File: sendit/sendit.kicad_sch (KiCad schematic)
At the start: 11 parts

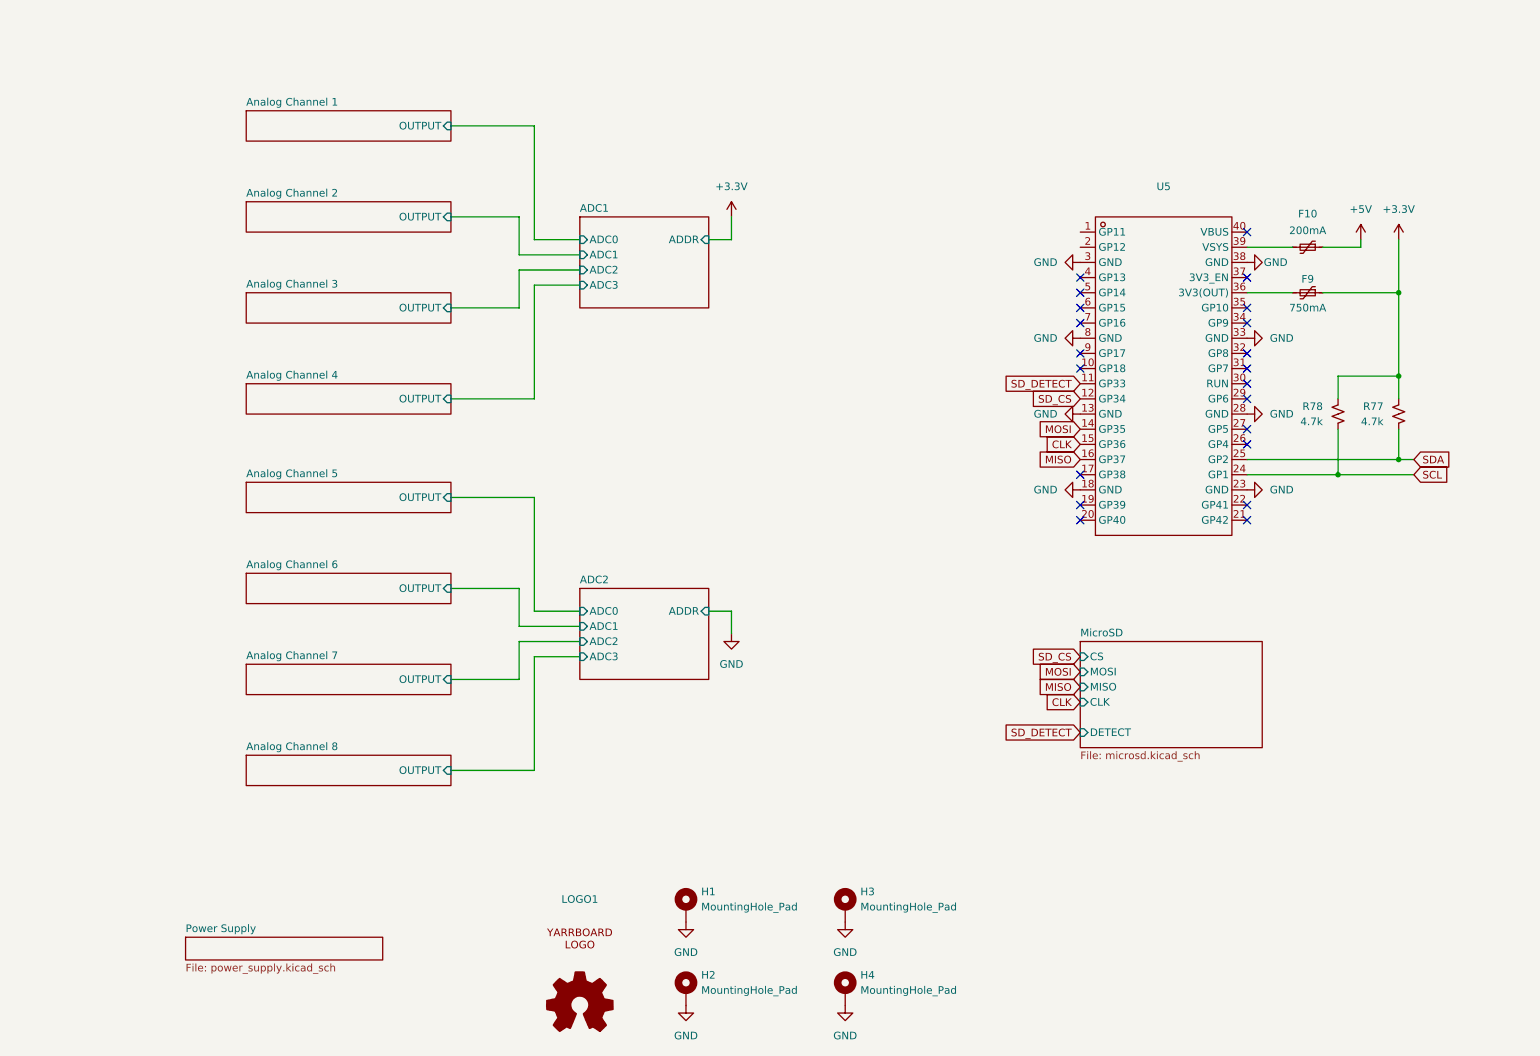
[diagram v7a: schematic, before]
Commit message: test run of jlcpcb upload looks good.
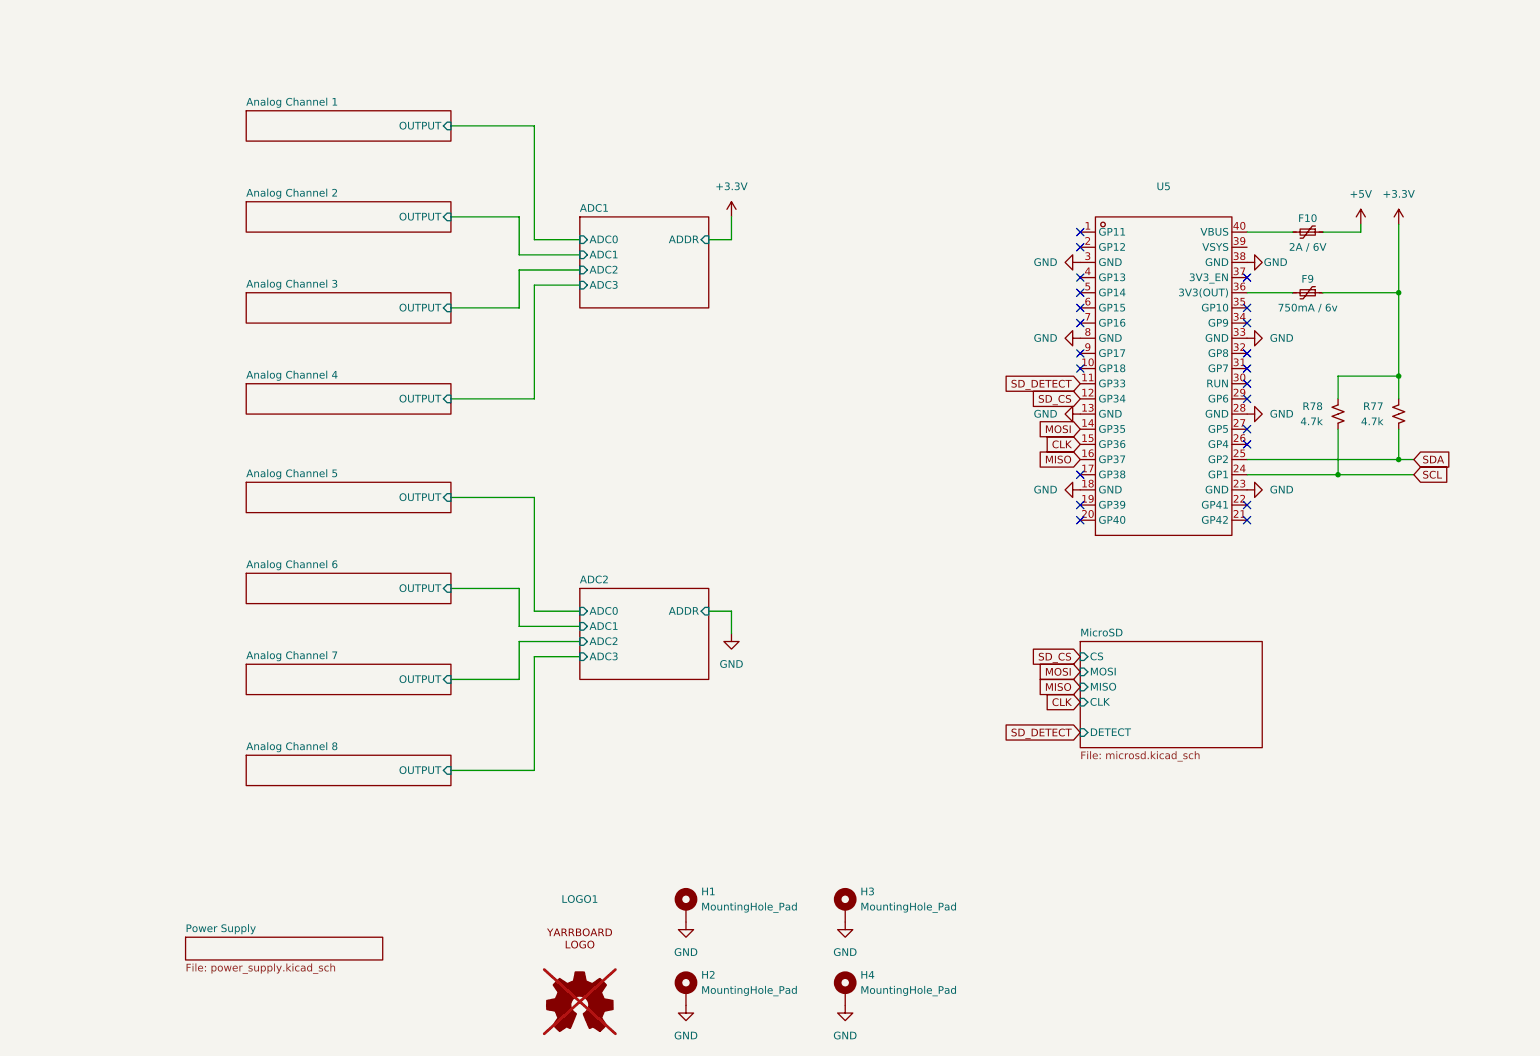
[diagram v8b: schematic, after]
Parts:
- F10: value 200mA -> 2A / 6V; LCSC C126816 -> C914095
- F9: value 750mA -> 750mA / 6v
- LOGO1, LOGO2: now not fitted
- R77, R78: LCSC (none) -> C23162
- U5: LCSC (none) -> C18198404
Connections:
- net at U5.39 (VSYS): no longer F10.2
- net at U5.40 (VBUS): now also F10.2
- no-connect marks 21 -> 22
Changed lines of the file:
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@@
+	)
+	(no_connect
+		(at 191.77 62.23)
 	)
 	(no_connect
@@
 	)
 	(no_connect
-		(at 219.71 59.69)
+		(at 191.77 59.69)
 	)
 	(no_connect
@@
 	(wire
 		(pts
-			(xy 219.71 62.23) (xy 227.33 62.23)
+			(xy 219.71 59.69) (xy 227.33 59.69)
 		)
 		(stroke
@@
 	(wire
 		(pts
-			(xy 238.76 62.23) (xy 238.76 60.96)
-		)
-		(stroke
-			(width 0)
-			(type default)
-		)
-	)
-	(wire
-		(pts
-			(xy 232.41 62.23) (xy 238.76 62.23)
+			(xy 238.76 59.69) (xy 238.76 58.42)
+		)
+		(stroke
+			(width 0)
+			(type default)
+		)
+	)
+	(wire
+		(pts
+			(xy 232.41 59.69) (xy 238.76 59.69)
 		)
 		(stroke
@@
 	(wire
 		(pts
-			(xy 245.11 60.96) (xy 245.11 69.85)
+			(xy 245.11 58.42) (xy 245.11 69.85)
 		)
 		(stroke
@@
 			)
 		)
-		(property "LCSC" ""
+		(property "LCSC" "C23162"
 			(at 234.95 90.17 0)
 			(effects
@@
 			)
 		)
+		(property "LCSC" "C18198404"
+			(at 205.74 83.82 0)
+			(effects
+				(font
+					(size 1.27 1.27)
+				)
+				(hide yes)
+			)
+		)
 		(pin "3"
 		)
@@
 		(in_bom no)
 		(on_board yes)
-		(dnp no)
+		(dnp yes)
 		(fields_autoplaced yes)
 		(property "Reference" "LOGO1"
@@
 	(symbol
 		(lib_id "power:+5V")
-		(at 238.76 60.96 0)
+		(at 238.76 58.42 0)
 		(mirror y)
 		(unit 1)
@@
 		(on_board yes)
 		(dnp no)
-		(fields_autoplaced yes)
 		(property "Reference" "#PWR03"
-			(at 238.76 64.77 0)
+			(at 238.76 62.23 0)
 			(effects
 				(font
@@
 		)
 		(property "Value" "+5V"
-			(at 238.76 55.88 0)
+			(at 238.76 53.34 0)
 			(effects
 				(font
@@
 		)
 		(property "Footprint" ""
-			(at 238.76 60.96 0)
+			(at 238.76 58.42 0)
 			(effects
 				(font
@@
 		)
 		(property "Datasheet" ""
-			(at 238.76 60.96 0)
+			(at 238.76 58.42 0)
 			(effects
 				(font
@@
 		)
 		(property "Description" "Power symbol creates a global label with name \"+5V\""
-			(at 238.76 60.96 0)
+			(at 238.76 58.42 0)
 			(effects
 				(font
@@
 	)
 	(symbol
+		(lib_id "Device:Polyfuse_Small")
+		(at 229.87 59.69 270)
+		(unit 1)
+		(exclude_from_sim no)
+		(in_bom yes)
+		(on_board yes)
+		(dnp no)
+		(property "Reference" "F10"
+			(at 229.87 57.404 90)
+			(effects
+				(font
+					(size 1.27 1.27)
+				)
+			)
+		)
+		(property "Value" "2A / 6V"
+			(at 229.87 62.23 90)
+			(effects
+				(font
+					(size 1.27 1.27)
+				)
+			)
+		)
+		(property "Footprint" "Fuse:Fuse_0805_2012Metric"
+			(at 224.79 60.96 0)
+			(effects
+				(font
+					(size 1.27 1.27)
+				)
+				(justify left)
+				(hide yes)
+			)
+		)
+		(property "Datasheet" "~"
+			(at 229.87 59.69 0)
+			(effects
+				(font
+					(size 1.27 1.27)
+				)
+				(hide yes)
+			)
+		)
+		(property "Description" ""
+			(at 229.87 59.69 0)
+			(effects
+				(font
+					(size 1.27 1.27)
+				)
+				(hide yes)
+			)
+		)
+		(property "LCSC" "C914095"
+			(at 229.87 59.69 90)
+			(effects
+				(font
+					(size 1.27 1.27)
+				)
+				(hide yes)
+			)
+		)
+		(pin "1"
+		)
+		(pin "2"
+		)
+		(instances
+			(project "sendit"
+				(path "/a355e4d0-2918-44fc-be8d-2503b84c6d6c"
+					(reference "F10")
+					(unit 1)
+				)
+			)
+		)
+	)
+	(symbol
 		(lib_id "power:GND")
 		(at 219.71 102.87 90)
@@
 		(exclude_from_sim yes)
 		(in_bom no)
-		(on_board no)
-		(dnp no)
+		(on_board yes)
+		(dnp yes)
 		(fields_autoplaced yes)
 		(property "Reference" "LOGO2"
@@
 	(symbol
 		(lib_id "power:+3.3V")
-		(at 245.11 60.96 0)
+		(at 245.11 58.42 0)
 		(unit 1)
 		(exclude_from_sim no)
@@
 		(on_board yes)
 		(dnp no)
-		(fields_autoplaced yes)
 		(property "Reference" "#PWR04"
-			(at 245.11 64.77 0)
+			(at 245.11 62.23 0)
 			(effects
 				(font
@@
 		)
 		(property "Value" "+3.3V"
-			(at 245.11 55.88 0)
+			(at 245.11 53.34 0)
 			(effects
 				(font
@@
 		)
 		(property "Footprint" ""
-			(at 245.11 60.96 0)
+			(at 245.11 58.42 0)
 			(effects
 				(font
@@
 		)
 		(property "Datasheet" ""
-			(at 245.11 60.96 0)
+			(at 245.11 58.42 0)
 			(effects
 				(font
@@
 		)
 		(property "Description" "Power symbol creates a global label with name \"+3.3V\""
-			(at 245.11 60.96 0)
+			(at 245.11 58.42 0)
 			(effects
 				(font
@@
 			)
 		)
-		(property "LCSC" ""
+		(property "LCSC" "C23162"
 			(at 245.11 90.17 0)
 			(effects
@@
 	)
 	(symbol
-		(lib_id "Device:Polyfuse_Small")
-		(at 229.87 62.23 270)
-		(unit 1)
-		(exclude_from_sim no)
-		(in_bom yes)
-		(on_board yes)
-		(dnp no)
-		(property "Reference" "F10"
-			(at 229.87 56.642 90)
-			(effects
-				(font
-					(size 1.27 1.27)
-				)
-			)
-		)
-		(property "Value" "200mA"
-			(at 229.87 59.436 90)
-			(effects
-				(font
-					(size 1.27 1.27)
-				)
-			)
-		)
-		(property "Footprint" "Fuse:Fuse_0805_2012Metric"
-			(at 224.79 63.5 0)
-			(effects
-				(font
-					(size 1.27 1.27)
-				)
-				(justify left)
-				(hide yes)
-			)
-		)
-		(property "Datasheet" "~"
-			(at 229.87 62.23 0)
-			(effects
-				(font
-					(size 1.27 1.27)
-				)
-				(hide yes)
-			)
-		)
-		(property "Description" ""
-			(at 229.87 62.23 0)
-			(effects
-				(font
-					(size 1.27 1.27)
-				)
-				(hide yes)
-			)
-		)
-		(property "LCSC" "C126816"
-			(at 229.87 62.23 90)
-			(effects
-				(font
-					(size 1.27 1.27)
-				)
-				(hide yes)
-			)
-		)
-		(pin "1"
-		)
-		(pin "2"
-		)
-		(instances
-			(project "sendit"
-				(path "/a355e4d0-2918-44fc-be8d-2503b84c6d6c"
-					(reference "F10")
-					(unit 1)
-				)
-			)
-		)
-	)
-	(symbol
 		(lib_id "power:GND")
 		(at 219.71 90.17 90)
@@
 			)
 		)
-		(property "Value" "750mA"
+		(property "Value" "750mA / 6v"
 			(at 229.87 72.39 90)
 			(effects
